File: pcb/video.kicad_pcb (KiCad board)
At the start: 4 copper layers, 159.9 x 99.9 mm, 174 parts, among them J1 09031966921, J3 Conn_01x06, J4 Conn_01x06, J5 Conn_01x06, J6 Conn_01x06, J7 DB15_Female_HighDensity, J8 HDMI_A, U1 NCP115, U10 NCA9306DPH, U2 LP3853ESX-3.3/NOPB, U3 LCMXO2-1200HC-4TG100I, U4 LCMXO2-7000HC-4TG144C, U5 THS8136, U6 TFP410PAP, U7 ESD224DQA, U8 ESD224DQA, U9 PCA9540BDP, X1 ASV-xxxMHz

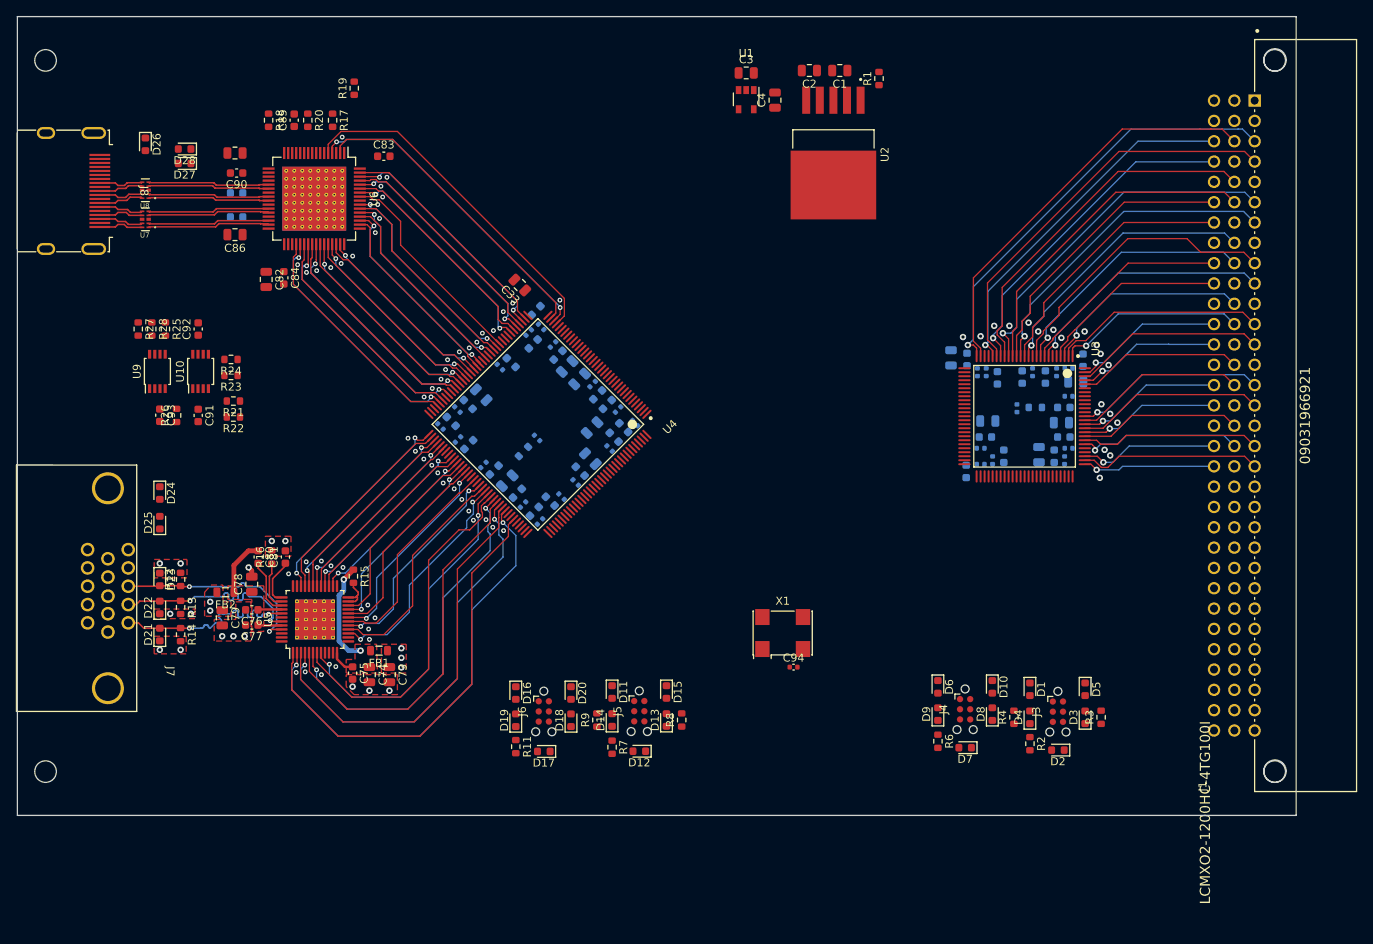
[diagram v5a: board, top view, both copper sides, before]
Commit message: add dualport ram for debug purposes
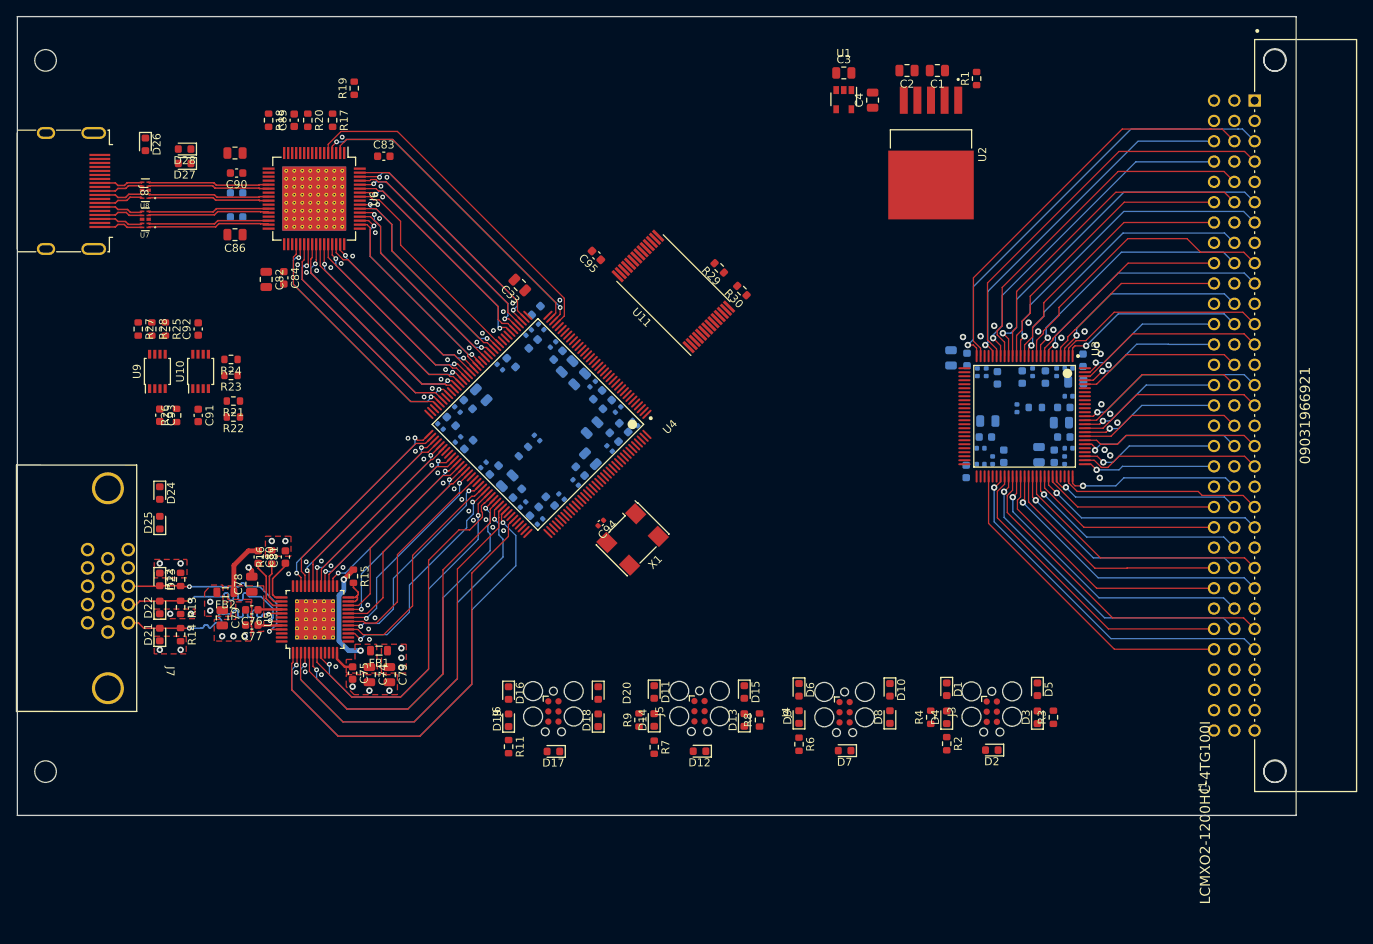
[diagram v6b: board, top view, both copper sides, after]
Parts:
- added C95: 100n, Capacitor_SMD:C_0603_1608Metric, F.Cu at (127.5, 74.9)
- added R29: 10k, Resistor_SMD:R_0603_1608Metric, F.Cu at (142.8, 76.5)
- added R30: 10k, Resistor_SMD:R_0603_1608Metric, F.Cu at (145.6, 79.3)
- added U11: S62LV256AL-45TLI, Package_SO:TSOP-I-28_11.8x8mm_P0.55mm, F.Cu at (137.1, 79.4)
- J3, J4, J5, J6: footprint Connector:Tag-Connect_TC2030-IDC-NL_2x03_P1.27mm_Vertical -> Connector:Tag-Connect_TC2030-IDC-FP_2x03_P1.27mm_Vertical
- moved C94 30.1 mm to (128.0, 108.4), turned to -135 degrees
- moved X1 22.1 mm to (132.0, 110.4), turned to -135 degrees
- moved D6 17.4 mm to (152.8, 129.2)
- moved D9 17.4 mm to (152.8, 132.6)
- moved R6 17.4 mm to (152.8, 136.0)
- moved D7 15.1 mm to (158.5, 136.8)
- moved J4 15.1 mm to (158.5, 132.0)
- moved D10 12.8 mm to (164.1, 129.2)
- moved D8 12.8 mm to (164.1, 132.6)
- moved C1 12.2 mm to (170.1, 51.8)
- moved C2 12.2 mm to (166.3, 51.8)
- moved C3 12.2 mm to (158.4, 52.1)
- moved C4 12.2 mm to (162.0, 55.5)
- moved R1 12.2 mm to (175.0, 52.8)
- moved U1 12.2 mm to (158.4, 54.3)
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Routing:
- net CONN_51: track 0.00 -> 45.2 mm, vias 0 -> 1
- net CONN_48: track 0.00 -> 41.7 mm
- net CONN_52: track 0.00 -> 41.2 mm
- net CONN_49: track 0.00 -> 39.9 mm, vias 0 -> 1
- net CONN_50: track 0.00 -> 38.4 mm
- net CONN_47: track 0.00 -> 37.3 mm, vias 0 -> 1
- net CONN_45: track 0.00 -> 36.8 mm, vias 0 -> 1
- net CONN_42: track 0.00 -> 33.3 mm
- net CONN_46: track 0.00 -> 32.9 mm
- net CONN_43: track 0.00 -> 31.5 mm, vias 0 -> 1
- net CONN_44: track 0.00 -> 29.8 mm
- net CONN_39: track 0.00 -> 29.0 mm, vias 0 -> 1
- net CONN_41: track 0.00 -> 29.0 mm, vias 0 -> 1
- net CONN_36: track 0.00 -> 25.3 mm
- net CONN_40: track 0.00 -> 24.7 mm
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
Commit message: route sram
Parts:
- moved C95 20.0 mm to (143.8, 86.4), turned to -45 degrees
- moved R29 11.1 mm to (142.6, 87.6)
- moved R30 10.5 mm to (141.4, 88.9)
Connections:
- U4 pad 10: unconnected-(U4F-PL8B) -> DPSRAM_A14
- U4 pad 11: unconnected-(U4F-PL9A) -> DPSRAM_A12
- U4 pad 12: unconnected-(U4F-PL9B) -> DPSRAM_A7
- U4 pad 13: unconnected-(U4E-PL10A) -> DPSRAM_A6
- U4 pad 14: unconnected-(U4E-PL10B) -> DPSRAM_A5
- U4 pad 15: unconnected-(U4E-PL11A) -> DPSRAM_A4
- U4 pad 17: unconnected-(U4E-PL11B) -> DPSRAM_A3
- U4 pad 19: unconnected-(U4E-PL12A/PCLKT4_0) -> DPSRAM_A2
- U4 pad 2: unconnected-(U4F-PL3B/L_GPLLC_FB) -> DPSRAM_OE
- U4 pad 20: unconnected-(U4E-PL12B/PCLKC4_0) -> DPSRAM_A1
- U4 pad 21: unconnected-(U4E-PL15A) -> DPSRAM_A0
- U4 pad 22: unconnected-(U4E-PL15B) -> DPSRAM_IO0
- U4 pad 23: unconnected-(U4E-PL17A) -> DPSRAM_IO1
- U4 pad 24: unconnected-(U4E-PL17B) -> DPSRAM_IO2
- U4 pad 25: unconnected-(U4D-PL19A) -> DPSRAM_IO3
- U4 pad 26: unconnected-(U4D-PL19B) -> DPSRAM_IO4
- U4 pad 27: unconnected-(U4D-PL22A/PCLKT3_0) -> DPSRAM_IO5
- U4 pad 28: unconnected-(U4D-PL22B/PCLKC3_0) -> DPSRAM_IO6
- U4 pad 3: unconnected-(U4F-PL4A/L_GPLLT_IN) -> DPSRAM_A11
- U4 pad 31: unconnected-(U4D-PL23D) -> DPSRAM_IO7
- U4 pad 32: unconnected-(U4D-PL24A) -> DPSRAM_A10
- U4 pad 4: unconnected-(U4F-PL4B/L_GPLLC_IN) -> DPSRAM_A9
- U4 pad 5: unconnected-(U4F-PL6A/PCLKT5_0) -> DPSRAM_A8
- U4 pad 6: unconnected-(U4F-PL6B/PCLKC5_0) -> DPSRAM_A13
- U4 pad 9: unconnected-(U4F-PL8A) -> DPSRAM_WE
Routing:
- net DPSRAM_A3: track 0.00 -> 20.1 mm
- net DPSRAM_A2: track 0.00 -> 19.8 mm
- net DPSRAM_A4: track 0.00 -> 19.6 mm
- net DPSRAM_A1: track 0.00 -> 19.1 mm
- net DPSRAM_A5: track 0.00 -> 18.9 mm
- net DPSRAM_A0: track 0.00 -> 18.3 mm
- net DPSRAM_A6: track 0.00 -> 18.2 mm
- net DPSRAM_IO0: track 0.00 -> 17.6 mm
- net DPSRAM_A7: track 0.00 -> 17.5 mm
- net DPSRAM_IO1: track 0.00 -> 16.9 mm
- net DPSRAM_A12: track 0.00 -> 16.8 mm
- net DPSRAM_IO2: track 0.00 -> 16.2 mm
- net DPSRAM_A14: track 0.00 -> 16.1 mm
- net DPSRAM_IO3: track 0.00 -> 15.1 mm
- net DPSRAM_WE: track 0.00 -> 14.9 mm
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
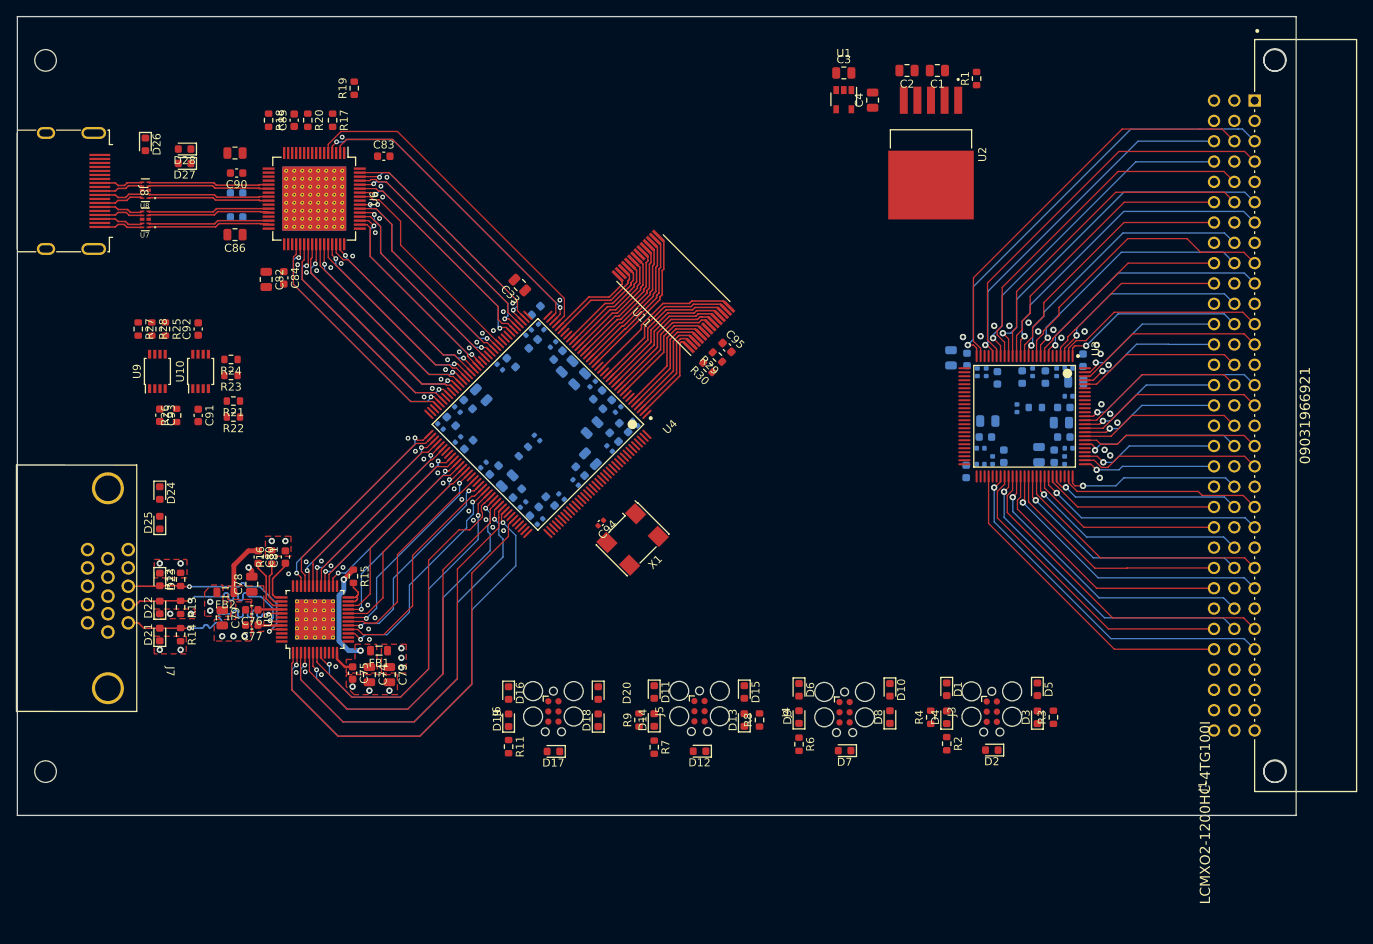
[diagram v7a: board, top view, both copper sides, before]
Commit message: add length matching to parallel buses
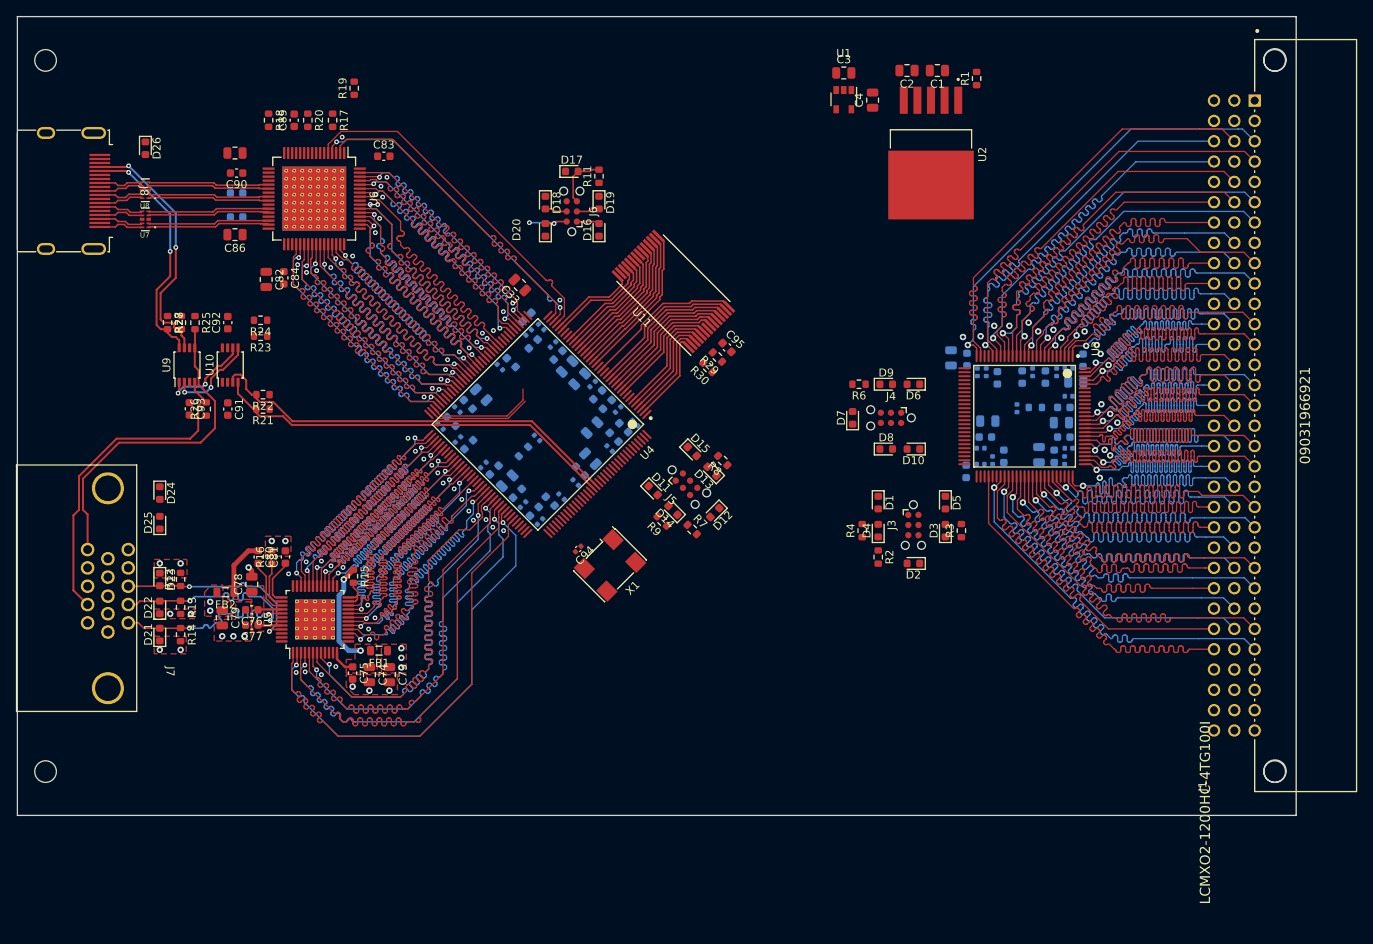
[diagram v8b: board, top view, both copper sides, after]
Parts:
- removed D27, D28: D_TVS, Diode_SMD:D_0603_1608Metric
- J3, J4, J5, J6: footprint Connector:Tag-Connect_TC2030-IDC-FP_2x03_P1.27mm_Vertical -> Connector:Tag-Connect_TC2030-IDC-NL_2x03_P1.27mm_Vertical
- moved D17 72.5 mm to (124.4, 64.4), turned to 0 degrees
- moved R11 72.2 mm to (127.8, 65.0), turned to 90 degrees
- moved D19 65.7 mm to (127.8, 68.3), turned to -90 degrees
- moved D18 65.0 mm to (121.1, 68.3), turned to -90 degrees
- moved J6 62.5 mm to (124.4, 69.4), turned to 90 degrees
- moved D16 59.0 mm to (127.8, 71.7), turned to 90 degrees
- moved D20 58.3 mm to (121.1, 71.7), turned to 90 degrees
- moved R6 45.6 mm to (160.3, 91.0), turned to 180 degrees
- moved D9 43.0 mm to (163.7, 91.0), turned to 0 degrees
- moved D7 41.6 mm to (159.5, 95.2), turned to 90 degrees
- moved D6 40.8 mm to (167.1, 91.0), turned to 180 degrees
- moved J4 37.3 mm to (164.3, 95.2), turned to 180 degrees
- moved D8 33.5 mm to (163.7, 99.1), turned to 0 degrees
- moved R8 32.8 mm to (143.2, 100.6), turned to 135 degrees
- moved D13 31.4 mm to (141.9, 101.9), turned to 135 degrees
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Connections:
- C49 pad 1: +3V3 -> +1V8
- C50 pad 1: +3V3 -> +1V8
- C51 pad 1: +3V3 -> +1V8
- C52 pad 1: +3V3 -> +1V8
- C53 pad 1: +3V3 -> +1V8
- C54 pad 1: +3V3 -> +1V8
- C55 pad 1: +3V3 -> +1V8
- U4 pad 102: +3V3 -> +1V8
- U4 pad 79: +3V3 -> +1V8
- U4 pad 88: +3V3 -> +1V8
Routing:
- net FPGA_SCL: track 0.00 -> 52.8 mm
- net FPGA_SDA: track 0.00 -> 51.0 mm
- net VGA_DDC_SDA: track 0.00 -> 41.7 mm
- net VGA_DDC_SCL: track 0.00 -> 41.6 mm
- net CONN_34: track 16.6 -> 54.1 mm
- net VGA_G7: track 23.1 -> 60.4 mm
- net CONN_32: track 17.3 -> 54.2 mm
- net VGA_G5: track 23.6 -> 60.4 mm
- net CONN_28: track 17.5 -> 54.1 mm
- net CONN_22: track 18.0 -> 54.1 mm
- net CONN_26: track 18.2 -> 54.2 mm
- net VGA_R7: track 24.6 -> 60.3 mm
- net VGA_G3: track 24.8 -> 60.4 mm
- net CONN_29: track 20.3 -> 55.5 mm
- net CONN_20: track 18.9 -> 54.0 mm
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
